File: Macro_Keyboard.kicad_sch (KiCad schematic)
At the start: 20 parts, among them SW1 SW_Push, U1 STM32L432KCUx, U2 LD39050PU33R

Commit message: Add files via upload
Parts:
- added H1, H2, H3, H4: MountingHole_Pad, MountingHole:MountingHole_2.2mm_M2_DIN965_Pad, symbol Mechanical:MountingHole_Pad
- C1: footprint (none) -> Capacitor_SMD:C_0603_1608Metric_Pad1.08x0.95mm_HandSolder
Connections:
- net GND: now also H1.1, H2.1, H3.1, H4.1
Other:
- note added: "Pull-Up intern"
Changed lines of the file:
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@@
   (junction (at 217.805 50.8) (diameter 0) (color 0 0 0 0)
   )
+  (junction (at 165.735 140.97) (diameter 0) (color 0 0 0 0)
+  )
   (junction (at 227.33 127) (diameter 0) (color 0 0 0 0)
   )
+  (junction (at 165.735 135.255) (diameter 0) (color 0 0 0 0)
+  )
   (junction (at 237.49 127) (diameter 0) (color 0 0 0 0)
   )
@@
   )
   (junction (at 173.99 50.8) (diameter 0) (color 0 0 0 0)
+  )
+  (junction (at 165.735 147.32) (diameter 0) (color 0 0 0 0)
   )
   (junction (at 57.15 53.34) (diameter 0) (color 0 0 0 0)
@@
     (stroke (width 0) (type default))
   )
+  (wire (pts (xy 165.735 135.255) (xy 168.275 135.255))
+    (stroke (width 0) (type default))
+  )
   (wire (pts (xy 244.475 48.26) (xy 244.475 50.8))
     (stroke (width 0) (type default))
@@
     (stroke (width 0) (type default))
   )
+  (wire (pts (xy 165.735 140.97) (xy 165.735 135.255))
+    (stroke (width 0) (type default))
+  )
+  (wire (pts (xy 165.735 135.255) (xy 165.735 128.905))
+    (stroke (width 0) (type default))
+  )
   (wire (pts (xy 237.49 127) (xy 237.49 128.27))
     (stroke (width 0) (type default))
@@
     (stroke (width 0) (type default))
   )
+  (wire (pts (xy 165.735 140.97) (xy 168.275 140.97))
+    (stroke (width 0) (type default))
+  )
   (wire (pts (xy 173.99 50.8) (xy 180.34 50.8))
     (stroke (width 0) (type default))
@@
     (stroke (width 0) (type default))
   )
+  (wire (pts (xy 165.735 147.32) (xy 165.735 140.97))
+    (stroke (width 0) (type default))
+  )
+  (wire (pts (xy 165.735 149.225) (xy 165.735 147.32))
+    (stroke (width 0) (type default))
+  )
   (wire (pts (xy 57.15 53.34) (xy 57.15 55.88))
     (stroke (width 0) (type default))
@@
     (stroke (width 0) (type default))
   )
+  (wire (pts (xy 165.735 128.905) (xy 168.275 128.905))
+    (stroke (width 0) (type default))
+  )
   (wire (pts (xy 232.41 124.46) (xy 232.41 127))
     (stroke (width 0) (type default))
@@
     (stroke (width 0) (type default))
   )
+  (wire (pts (xy 165.735 147.32) (xy 168.275 147.32))
+    (stroke (width 0) (type default))
+  )
   (wire (pts (xy 29.21 63.5) (xy 27.94 63.5))
     (stroke (width 0) (type default))
@@
   )
   (text "Linear Regler" (at 243.205 80.01 0)
+    (effects (font (size 1.27 1.27)) (justify left bottom))
+  )
+  (text "Pull-Up intern" (at 50.8 46.99 0)
     (effects (font (size 1.27 1.27)) (justify left bottom))
   )
@@
         (path "/41b3a189-fb3d-44ed-903d-e385e89f379a"
           (reference "#PWR016") (unit 1)
+        )
+      )
+    )
+  )
+  (symbol (lib_id "Mechanical:MountingHole_Pad") (at 170.815 135.255 270) (unit 1)
+    (in_bom yes) (on_board yes) (dnp no) (fields_autoplaced)
+    (property "Reference" "H2" (at 174.625 134.62 90)
+      (effects (font (size 1.27 1.27)) (justify left))
+    )
+    (property "Value" "MountingHole_Pad" (at 174.625 137.16 90)
+      (effects (font (size 1.27 1.27)) (justify left))
+    )
+    (property "Footprint" "MountingHole:MountingHole_2.2mm_M2_DIN965_Pad" (at 170.815 135.255 0)
+      (effects (font (size 1.27 1.27)) hide)
+    )
+    (property "Datasheet" "~" (at 170.815 135.255 0)
+      (effects (font (size 1.27 1.27)) hide)
+    )
+    (pin "1")
+    (instances
+      (project "Macro_Keyboard"
+        (path "/41b3a189-fb3d-44ed-903d-e385e89f379a/677311a0-3359-4839-9fb7-d21d36931826"
+          (reference "H2") (unit 1)
+        )
+        (path "/41b3a189-fb3d-44ed-903d-e385e89f379a"
+          (reference "H2") (unit 1)
         )
       )
@@
     )
   )
+  (symbol (lib_id "Mechanical:MountingHole_Pad") (at 170.815 128.905 270) (unit 1)
+    (in_bom yes) (on_board yes) (dnp no) (fields_autoplaced)
+    (property "Reference" "H1" (at 174.625 128.27 90)
+      (effects (font (size 1.27 1.27)) (justify left))
+    )
+    (property "Value" "MountingHole_Pad" (at 174.625 130.81 90)
+      (effects (font (size 1.27 1.27)) (justify left))
+    )
+    (property "Footprint" "MountingHole:MountingHole_2.2mm_M2_DIN965_Pad" (at 170.815 128.905 0)
+      (effects (font (size 1.27 1.27)) hide)
+    )
+    (property "Datasheet" "~" (at 170.815 128.905 0)
+      (effects (font (size 1.27 1.27)) hide)
+    )
+    (pin "1")
+    (instances
+      (project "Macro_Keyboard"
+        (path "/41b3a189-fb3d-44ed-903d-e385e89f379a/677311a0-3359-4839-9fb7-d21d36931826"
+          (reference "H1") (unit 1)
+        )
+        (path "/41b3a189-fb3d-44ed-903d-e385e89f379a"
+          (reference "H1") (unit 1)
+        )
+      )
+    )
+  )
   (symbol (lib_id "Device:C") (at 217.805 55.88 0) (unit 1)
     (in_bom yes) (on_board yes) (dnp no) (fields_autoplaced)
@@
         (path "/41b3a189-fb3d-44ed-903d-e385e89f379a"
           (reference "TP1") (unit 1)
+        )
+      )
+    )
+  )
+  (symbol (lib_id "Mechanical:MountingHole_Pad") (at 170.815 147.32 270) (unit 1)
+    (in_bom yes) (on_board yes) (dnp no) (fields_autoplaced)
+    (property "Reference" "H4" (at 175.26 146.685 90)
+      (effects (font (size 1.27 1.27)) (justify left))
+    )
+    (property "Value" "MountingHole_Pad" (at 175.26 149.225 90)
+      (effects (font (size 1.27 1.27)) (justify left))
+    )
+    (property "Footprint" "MountingHole:MountingHole_2.2mm_M2_DIN965_Pad" (at 170.815 147.32 0)
+      (effects (font (size 1.27 1.27)) hide)
+    )
+    (property "Datasheet" "~" (at 170.815 147.32 0)
+      (effects (font (size 1.27 1.27)) hide)
+    )
+    (pin "1")
+    (instances
+      (project "Macro_Keyboard"
+        (path "/41b3a189-fb3d-44ed-903d-e385e89f379a/677311a0-3359-4839-9fb7-d21d36931826"
+          (reference "H4") (unit 1)
+        )
+        (path "/41b3a189-fb3d-44ed-903d-e385e89f379a"
+          (reference "H4") (unit 1)
         )
       )
@@
         (path "/41b3a189-fb3d-44ed-903d-e385e89f379a"
           (reference "R3") (unit 1)
+        )
+      )
+    )
+  )
+  (symbol (lib_id "power:GND") (at 165.735 149.225 0) (unit 1)
+    (in_bom yes) (on_board yes) (dnp no) (fields_autoplaced)
+    (property "Reference" "#PWR091" (at 165.735 155.575 0)
+      (effects (font (size 1.27 1.27)) hide)
+    )
+    (property "Value" "GND" (at 165.735 153.67 0)
+      (effects (font (size 1.27 1.27)))
+    )
+    (property "Footprint" "" (at 165.735 149.225 0)
+      (effects (font (size 1.27 1.27)) hide)
+    )
+    (property "Datasheet" "" (at 165.735 149.225 0)
+      (effects (font (size 1.27 1.27)) hide)
+    )
+    (pin "1")
+    (instances
+      (project "Macro_Keyboard"
+        (path "/41b3a189-fb3d-44ed-903d-e385e89f379a/677311a0-3359-4839-9fb7-d21d36931826"
+          (reference "#PWR091") (unit 1)
+        )
+        (path "/41b3a189-fb3d-44ed-903d-e385e89f379a"
+          (reference "#PWR091") (unit 1)
         )
       )
@@
       (effects (font (size 1.27 1.27)) (justify left))
     )
-    (property "Footprint" "" (at 181.3052 64.77 0)
+    (property "Footprint" "Capacitor_SMD:C_0603_1608Metric_Pad1.08x0.95mm_HandSolder" (at 181.3052 64.77 0)
       (effects (font (size 1.27 1.27)) hide)
     )
@@
         )
       )
+    )
+  )
+  (symbol (lib_id "Mechanical:MountingHole_Pad") (at 170.815 140.97 270) (unit 1)
+    (in_bom yes) (on_board yes) (dnp no) (fields_autoplaced)
+    (property "Reference" "H3" (at 175.26 140.335 90)
+      (effects (font (size 1.27 1.27)) (justify left))
+    )
+    (property "Value" "MountingHole_Pad" (at 175.26 142.875 90)
+      (effects (font (size 1.27 1.27)) (justify left))
+    )
+    (property "Footprint" "MountingHole:MountingHole_2.2mm_M2_DIN965_Pad" (at 170.815 140.97 0)
+      (effects (font (size 1.27 1.27)) hide)
+    )
+    (property "Datasheet" "~" (at 170.815 140.97 0)
+      (effects (font (size 1.27 1.27)) hide)
+    )
+    (pin "1")
+    (instances
+      (project "Macro_Keyboard"
+        (path "/41b3a189-fb3d-44ed-903d-e385e89f379a/677311a0-3359-4839-9fb7-d21d36931826"
+          (reference "H3") (unit 1)
+        )
+        (path "/41b3a189-fb3d-44ed-903d-e385e89f379a"
+          (reference "H3") (unit 1)
+        )
+      )

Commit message: Add files via upload
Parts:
- C17: footprint Capacitor_SMD:CP_Elec_4x5.8 -> Capacitor_SMD:C_0201_0603Metric_Pad0.64x0.40mm_HandSolder
- SW1: footprint Button_Switch_THT:SW_Tactile_SPST_Angled_PTS645Vx31-2LFS -> Button_Switch_THT:SW_Tactile_SKHH_Angled
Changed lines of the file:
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@@
       (effects (font (size 1.27 1.27)) (justify left))
     )
-    (property "Footprint" "Capacitor_SMD:CP_Elec_4x5.8" (at 240.03 55.88 0)
+    (property "Footprint" "Capacitor_SMD:C_0201_0603Metric_Pad0.64x0.40mm_HandSolder" (at 240.03 55.88 0)
       (effects (font (size 1.27 1.27)) hide)
     )
@@
       (effects (font (size 1.27 1.27)))
     )
-    (property "Footprint" "Button_Switch_THT:SW_Tactile_SPST_Angled_PTS645Vx31-2LFS" (at 22.86 55.88 0)
-      (effects (font (size 1.27 1.27)) hide)
-    )
+    (property "Footprint" "Button_Switch_THT:SW_Tactile_SKHH_Angled" (at 22.86 55.88 0)
+      (effects (font (size 1.27 1.27)) hide)
+    )

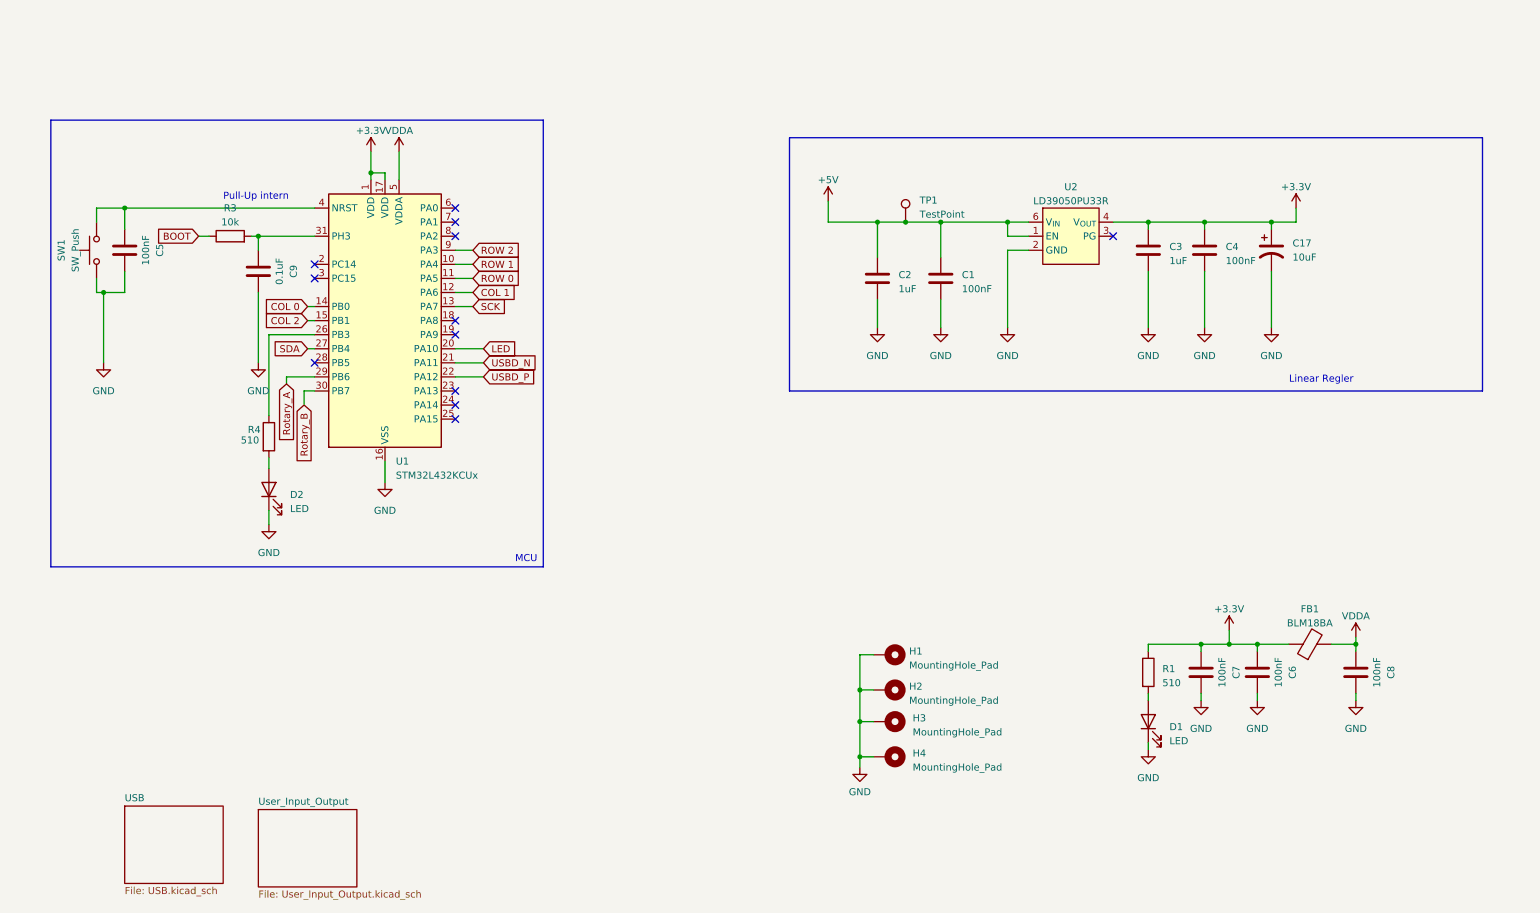
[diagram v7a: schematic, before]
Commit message: Add STM32 Symbol and changed schematic
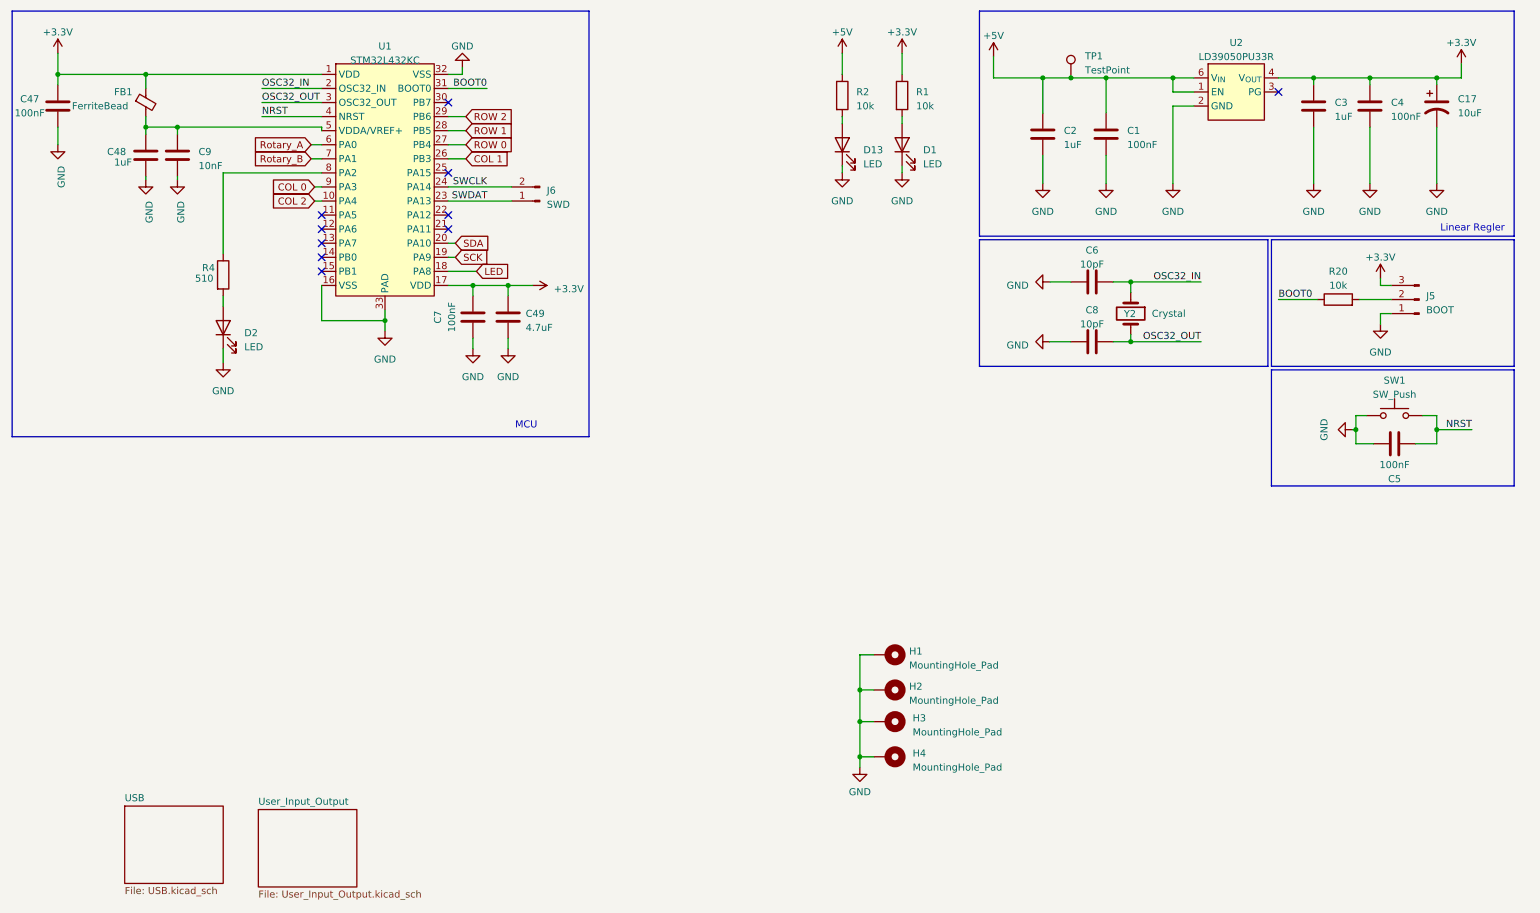
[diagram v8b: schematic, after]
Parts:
- removed FB1: BLM18BA, Inductor_SMD:L_0603_1608Metric_Pad1.05x0.95mm_HandSolder, symbol Device:FerriteBead
- removed R3: 10k, Resistor_SMD:R_0805_2012Metric_Pad1.20x1.40mm_HandSolder, symbol Device:R
- removed U1: STM32L432KCUx, Package_DFN_QFN:QFN-32-1EP_5x5mm_P0.5mm_EP3.45x3.45mm, symbol MCU_ST_STM32L4:STM32L432KCUx
- added C47: 100nF, Capacitor_SMD:C_0603_1608Metric_Pad1.08x0.95mm_HandSolder, symbol Device:C
- added C48: 1uF, symbol Device:C
- added C49: 4.7uF, symbol Device:C
- added D13: LED, LED_SMD:LED_0805_2012Metric_Pad1.15x1.40mm_HandSolder, symbol Device:LED
- added FB1: FerriteBead, symbol Device:FerriteBead_Small
- added J5: BOOT, symbol Connector:Conn_01x03_Pin
- added J6: SWD, symbol Connector:Conn_01x02_Pin
- added R2: 10k, Resistor_SMD:R_0805_2012Metric_Pad1.20x1.40mm_HandSolder, symbol Device:R
- added R20: 10k, symbol Device:R
- added U1: STM32L432KC, symbol STM32_L432K:STM32L432KC
- added Y2: Crystal, symbol Device:Crystal
- C6, C8: value 100nF -> 10pF; footprint Capacitor_SMD:C_0603_1608Metric_Pad1.08x0.95mm_HandSolder -> (none)
- C9: value 0.1uF -> 10nF; footprint Capacitor_SMD:C_0603_1608Metric_Pad1.08x0.95mm_HandSolder -> (none)
- R1: value 510 -> 10k
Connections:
- net VDDA is gone; now on net GND: C8.1
- net +3.3V: now also C7.2, C47.2, C49.2, FB1.1, J5.3 (Pin_3), U1.1 (VDD), U1.17 (VDD); no longer C6.1, C7.1
- net +5V: now also R2.1
- net COL 0: now also U1.9 (PA3)
- net COL 1: now also U1.26 (PB3)
- net COL 2: now also U1.10 (PA4)
- net GND: now also C6.1, C7.1, C47.1, C48.1, C49.1, D13.1 (K), J5.1 (Pin_1), U1.16 (VSS), U1.32 (VSS), U1.33 (PAD); no longer C6.2, C7.2, C8.2
- net LED: now also U1.18 (PA8)
- net ROW 0: now also U1.27 (PB4)
- net ROW 1: now also U1.28 (PB5)
- net ROW 2: now also U1.29 (PB6)
- net Rotary_A: now also U1.6 (PA0)
- net Rotary_B: now also U1.7 (PA1)
- net SCK: now also U1.19 (PA9)
- net SDA: now also U1.20 (PA10)
- net at R4.1: now also U1.8 (PA2)
- net at C9.1: now also C48.2, FB1.2, U1.5 (VDDA/VREF+)
- net NRST: now reaches C5.1, SW1.2
- net NRST: now also U1.4 (NRST)
- new net: D13.2 (A), R2.2
- new net: J5.2 (Pin_2), R20.2
- new net BOOT0: R20.1, U1.31 (BOOT0)
- new net OSC32_IN: C6.2, U1.2 (OSC32_IN), Y2.1
- new net OSC32_OUT: C8.2, U1.3 (OSC32_OUT), Y2.2
- new net SWCLK: J6.2 (Pin_2), U1.24 (PA14)
- new net SWDAT: J6.1 (Pin_1), U1.23 (PA13)
- no-connect marks 12 -> 10
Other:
- note removed: "Pull-Up intern"
- moved on the sheet: C1, C17, C2, C3, C4, C5, D1, D2, R1, R4, SW1, TP1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
